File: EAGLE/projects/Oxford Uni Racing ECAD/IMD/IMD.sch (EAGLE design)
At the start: 23 parts, among them IC1 LM2901N, IC2 NE555, J2 T821108A1S100CEU, K1 RT444012

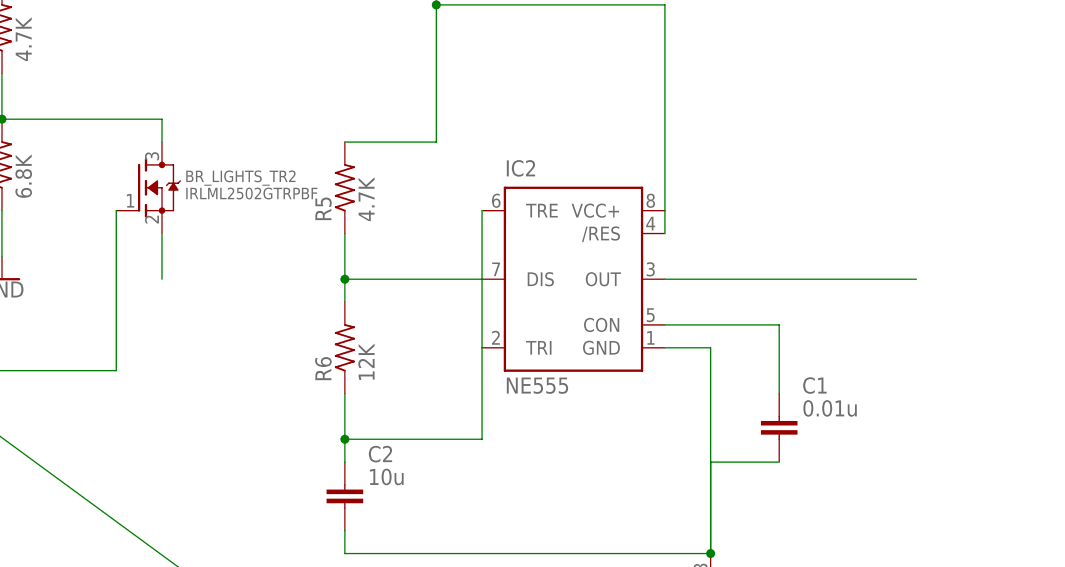
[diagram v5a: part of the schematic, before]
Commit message: Added name tags to outputs
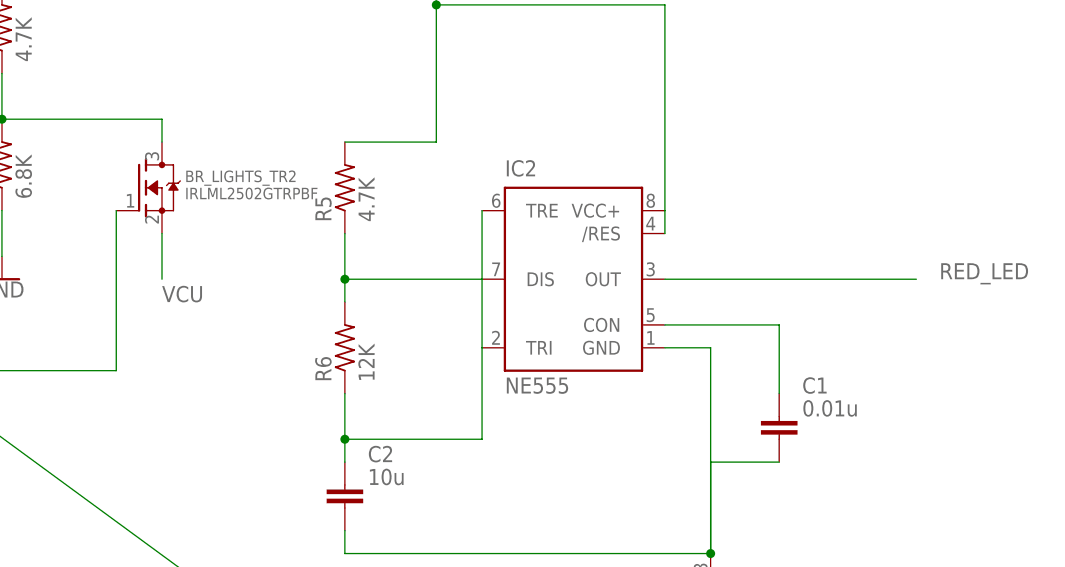
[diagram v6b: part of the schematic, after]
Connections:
- net N$13 renamed VCU
- net N$9 renamed RED_LED
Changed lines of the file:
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@@
 </segment>
 </net>
-<net name="N$9" class="0">
+<net name="RED_LED" class="0">
 <segment>
 <pinref part="IC2" gate="G$1" pin="OUT"/>
 <wire x1="228.6" y1="-48.26" x2="256.54" y2="-48.26" width="0.1524" layer="91"/>
+<label x="259.08" y="-48.26" size="1.778" layer="95"/>
 </segment>
 </net>
@@
 </segment>
 </net>
-<net name="N$13" class="0">
+<net name="VCU" class="0">
 <segment>
 <pinref part="BR_LIGHTS_TR2" gate="G$1" pin="S"/>
 <wire x1="172.72" y1="-43.18" x2="172.72" y2="-48.26" width="0.1524" layer="91"/>
+<label x="172.72" y="-50.8" size="1.778" layer="95"/>
 </segment>
 </net>

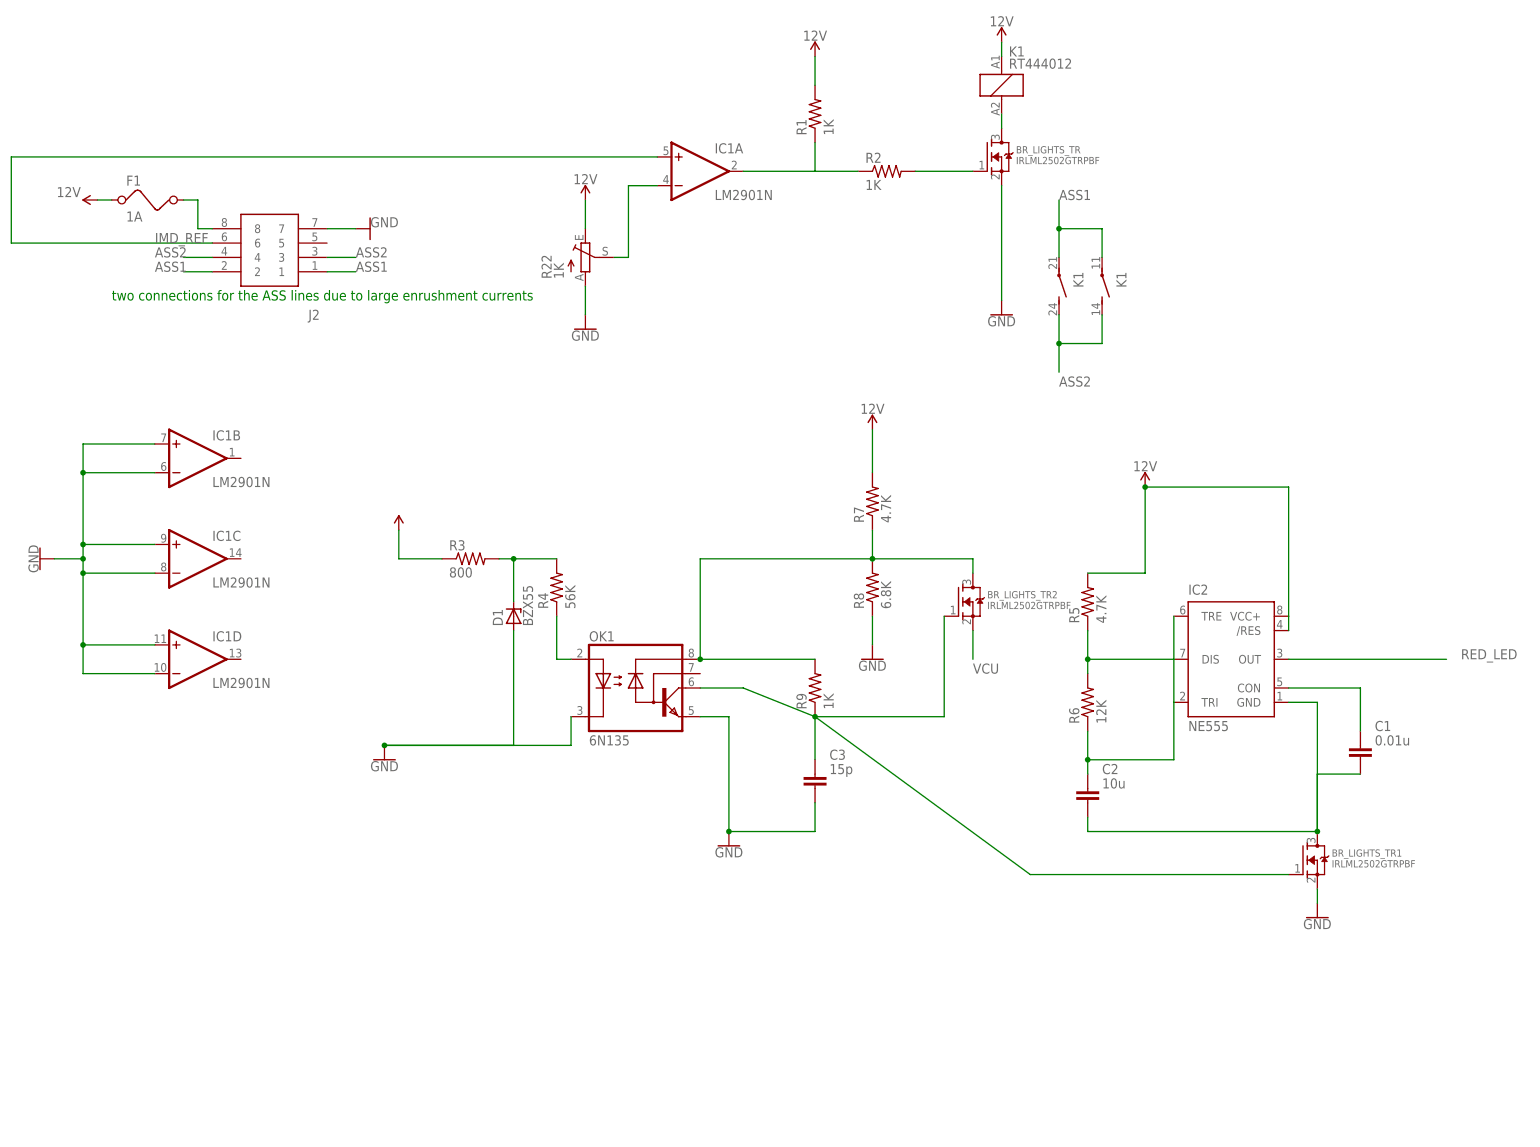
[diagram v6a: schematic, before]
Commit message: Second iteration of TSAL schematic
Added P-type MOSFET for green light, added labels for outputs
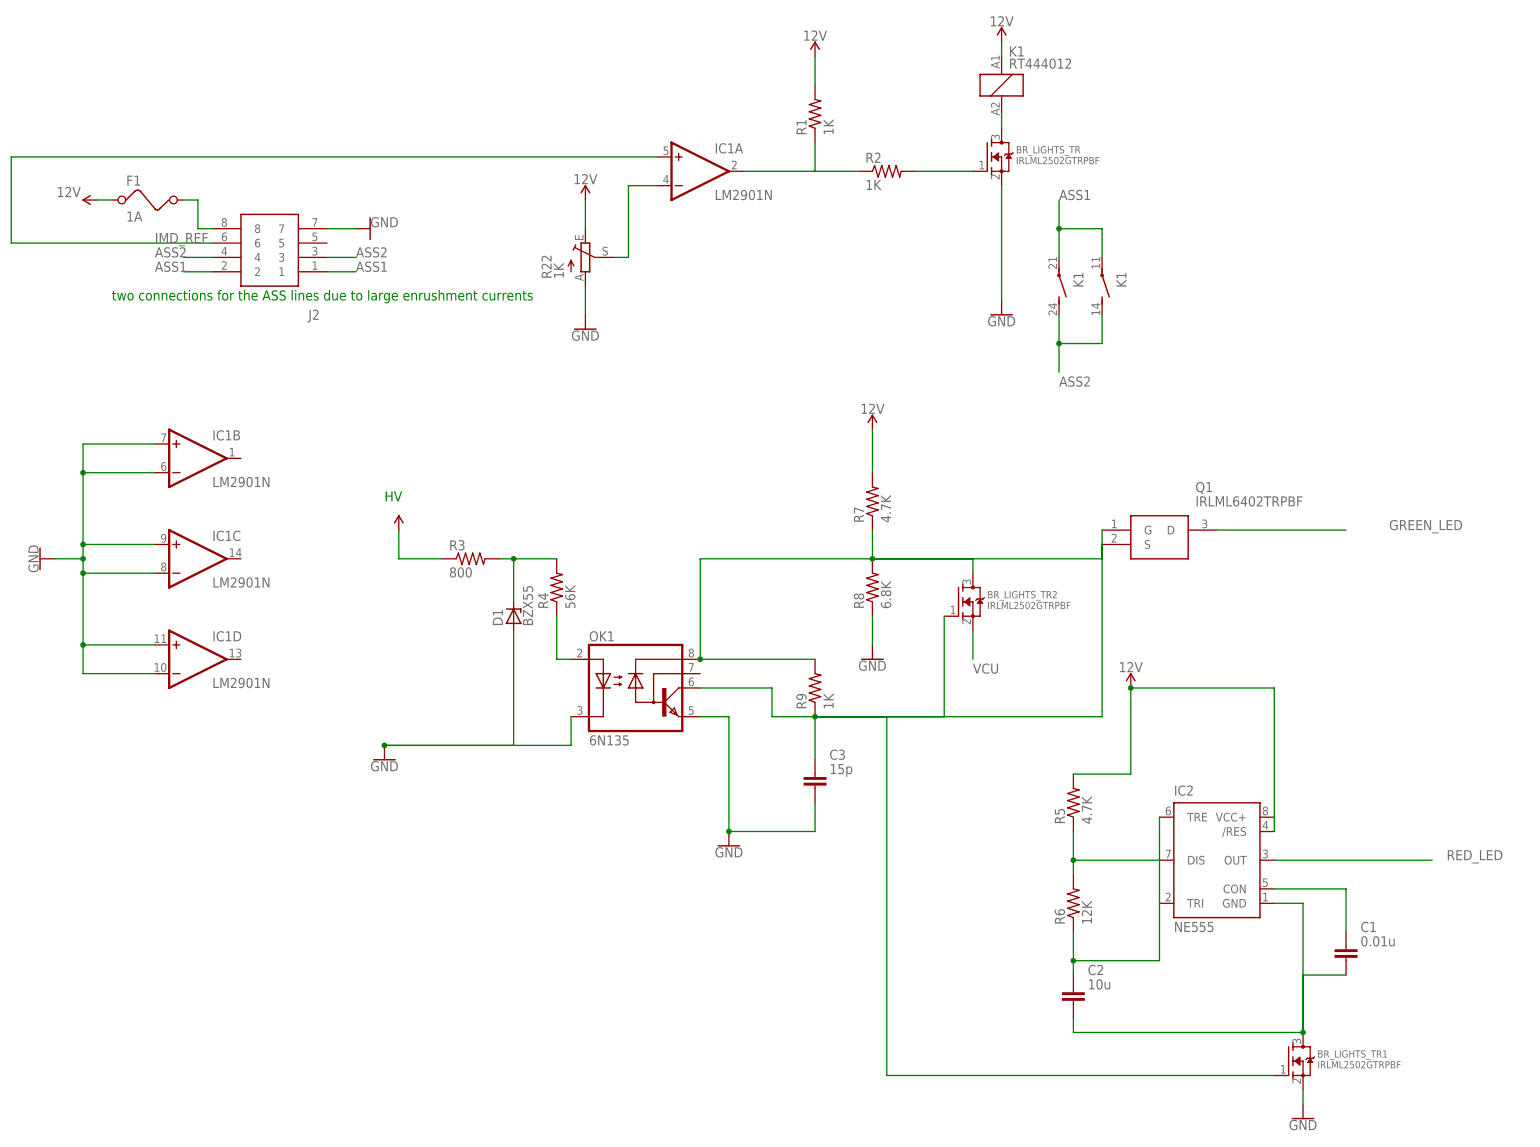
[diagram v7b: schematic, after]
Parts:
- added Q1: IRLML6402TRPBF, SamacSys_Parts:IRLML6402TRPBF
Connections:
- removed net N$17: BR_LIGHTS_TR1.G, BR_LIGHTS_TR2.G, C3.1, OK1.VO, R9.1
- new net GREEN_LED: Q1.D
- new net N$13: BR_LIGHTS_TR1.G, BR_LIGHTS_TR2.G, C3.1, OK1.VO, Q1.G, R9.1
- net N$16: now also Q1.S
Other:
- note added: "HV"
- moved on the sheet: BR_LIGHTS_TR1, C1, C2, IC2, R5, R6

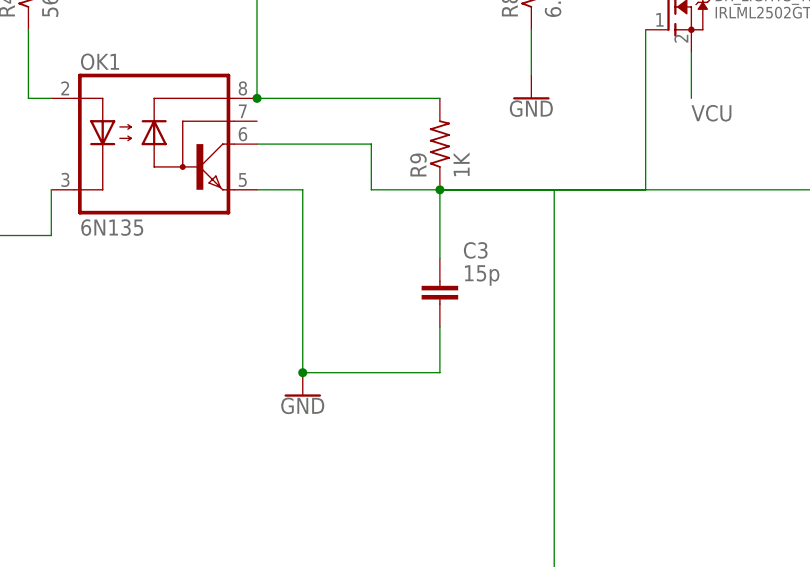
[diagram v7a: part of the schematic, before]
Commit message: Removed unnecessary capacitor from TSAL schematic
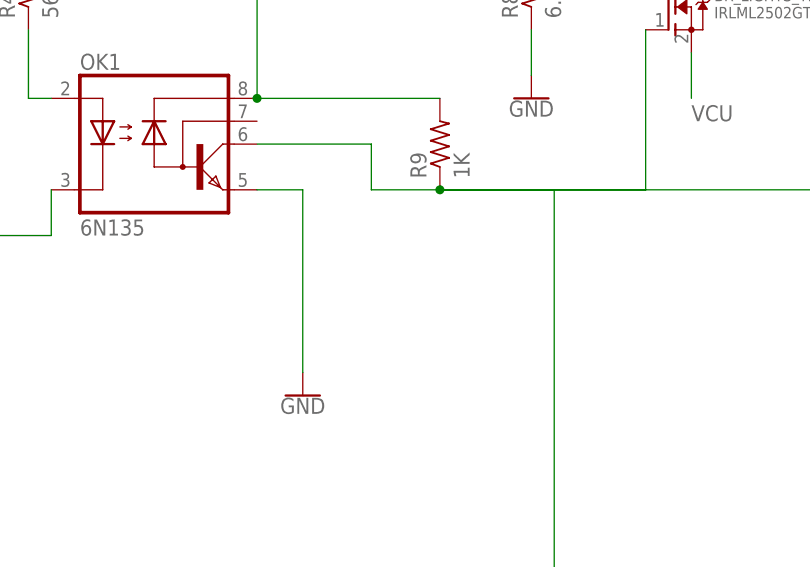
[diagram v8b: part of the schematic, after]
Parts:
- removed C3: 15p, ngspice-simulation:C
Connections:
- net GND: no longer C3.2
- net N$13: no longer C3.1
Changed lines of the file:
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@@
 <part name="GND7" library="SparkFun-PowerSymbols" library_urn="urn:adsk.eagle:library:530" deviceset="GND" device=""/>
 <part name="R9" library="adafruit" library_urn="urn:adsk.eagle:library:420" deviceset="R-US_" device="0204/7" package3d_urn="urn:adsk.eagle:package:6240596/1" value="1K"/>
-<part name="C3" library="ngspice-simulation" library_urn="urn:adsk.eagle:library:527439" deviceset="C" device="" value="15p"/>
 <part name="BR_LIGHTS_TR2" library="adafruit" library_urn="urn:adsk.eagle:library:420" deviceset="MOSFET-N" device="REFLOW" package3d_urn="urn:adsk.eagle:package:6240836/1" value="IRLML2502GTRPBF"/>
 <part name="Q1" library="SamacSys_Parts" deviceset="IRLML6402TRPBF" device=""/>
@@
 <attribute name="NAME" x="143.2814" y="-57.15" size="1.778" layer="95" rot="R90"/>
 <attribute name="VALUE" x="148.082" y="-57.15" size="1.778" layer="96" rot="R90"/>
-</instance>
-<instance part="C3" gate="G$1" x="144.78" y="-68.58" smashed="yes">
-<attribute name="NAME" x="147.32" y="-66.04" size="1.778" layer="95"/>
-<attribute name="VALUE" x="147.32" y="-68.58" size="1.778" layer="96"/>
 </instance>
 <instance part="BR_LIGHTS_TR2" gate="G$1" x="170.18" y="-38.1" smashed="yes">
@@
 <wire x1="124.46" y1="-58.42" x2="129.54" y2="-58.42" width="0.1524" layer="91"/>
 <wire x1="129.54" y1="-58.42" x2="129.54" y2="-78.74" width="0.1524" layer="91"/>
-<pinref part="C3" gate="G$1" pin="2"/>
-<wire x1="144.78" y1="-73.66" x2="144.78" y2="-78.74" width="0.1524" layer="91"/>
-<wire x1="144.78" y1="-78.74" x2="129.54" y2="-78.74" width="0.1524" layer="91"/>
-<junction x="129.54" y="-78.74"/>
 </segment>
 <segment>
@@
 <wire x1="137.16" y1="-53.34" x2="137.16" y2="-58.42" width="0.1524" layer="91"/>
 <pinref part="R9" gate="G$1" pin="1"/>
-<pinref part="C3" gate="G$1" pin="1"/>
-<wire x1="144.78" y1="-58.42" x2="144.78" y2="-66.04" width="0.1524" layer="91"/>
 <junction x="144.78" y="-58.42"/>
 <pinref part="BR_LIGHTS_TR2" gate="G$1" pin="G"/>
